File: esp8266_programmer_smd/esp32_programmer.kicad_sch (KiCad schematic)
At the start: 42 parts, among them P1 USB_C_Plug_USB2.0, Q1 S8050, Q2 S8050, SW1 SW_Push, SW2 SW_Push, U1 CH340C, U2 ESP-12E

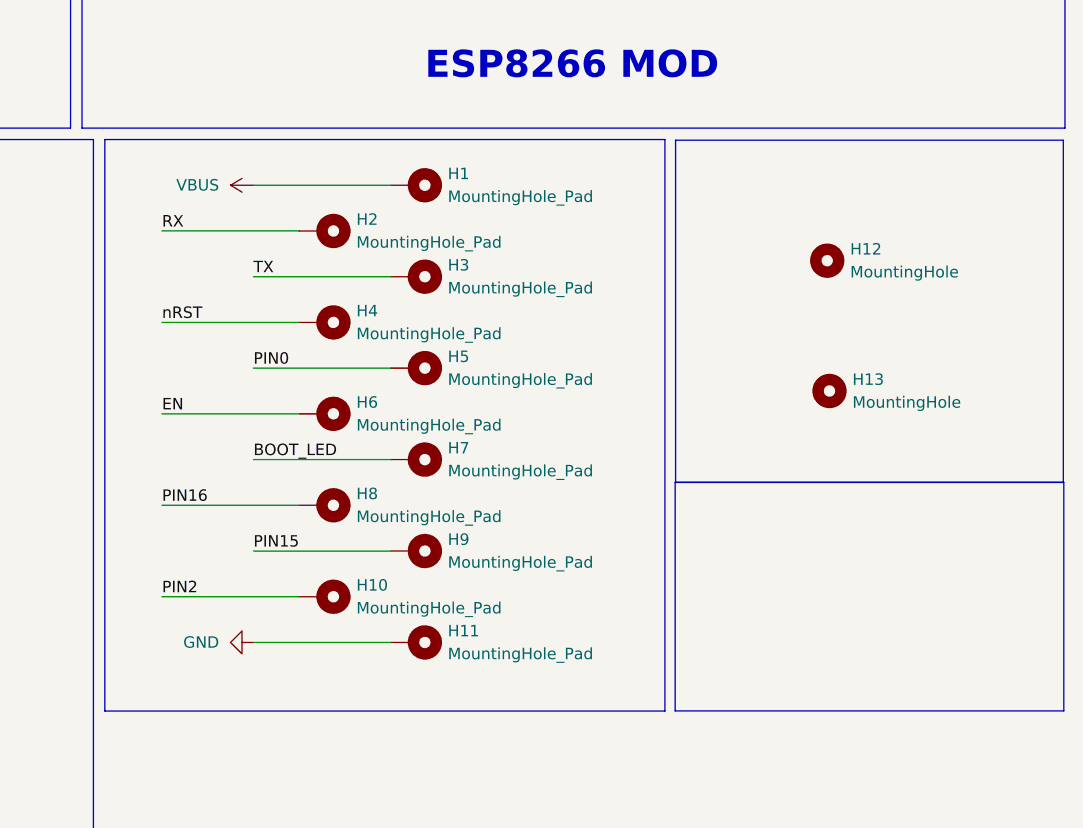
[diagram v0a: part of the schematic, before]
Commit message: Updated #6 pcb problem
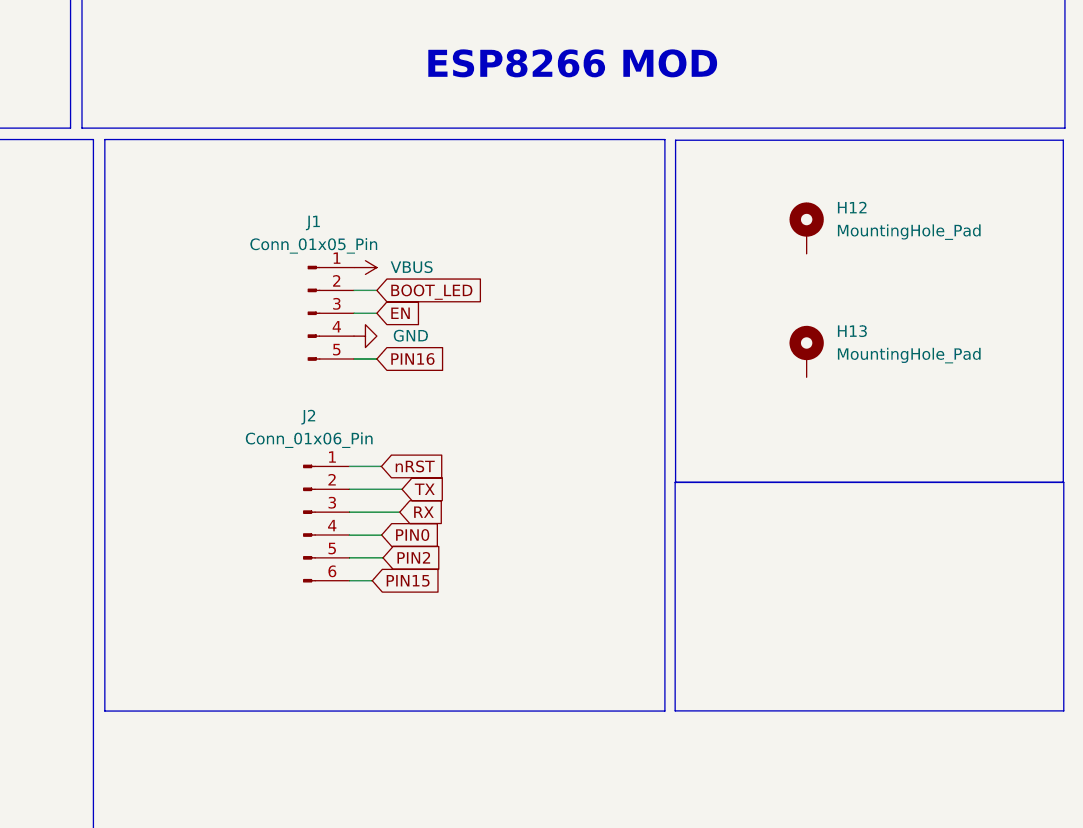
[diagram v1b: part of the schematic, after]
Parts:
- removed H1, H10, H11, H2, H3, H4, H5, H6, H7, H8, H9: MountingHole_Pad, Connector_PinHeader_1.00mm:PinHeader_1x01_P1.00mm_Vertical, symbol Mechanical:MountingHole_Pad
- removed H12, H13: MountingHole, MountingHole:MountingHole_2.5mm, symbol Mechanical:MountingHole
- added H12, H13: MountingHole_Pad, MountingHole:MountingHole_2.2mm_M2_Pad_Via, symbol Mechanical:MountingHole_Pad
- added J1: Conn_01x05_Pin, Connector_PinHeader_2.54mm:PinHeader_1x05_P2.54mm_Vertical, symbol Connector:Conn_01x05_Pin
- added J2: Conn_01x06_Pin, Connector_PinHeader_2.54mm:PinHeader_1x06_P2.54mm_Vertical, symbol Connector:Conn_01x06_Pin
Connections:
- net BOOT_LED: now also J1.2 (Pin_2)
- net EN: now also J1.3 (Pin_3)
- net GND: now also J1.4 (Pin_4)
- net PIN0: now also J2.4 (Pin_4)
- net PIN15: now also J2.6 (Pin_6)
- net PIN16: now also J1.5 (Pin_5)
- net PIN2: now also J2.5 (Pin_5)
- net RX: now also J2.3 (Pin_3)
- net TX: now also J2.2 (Pin_2)
- net VBUS: now also J1.1 (Pin_1)
- net nRST: now also J2.1 (Pin_1)
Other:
- company: (none) -> Zheng Lin Lei
- title: (none) -> esp8266 programmer
